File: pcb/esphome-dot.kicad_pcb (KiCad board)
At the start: 4 copper layers, 77 x 75.8 mm, 7 parts, among them J1 Input, J2 Even, J3 Odd, J4 Output, J5 SPK1, J6 SPK2

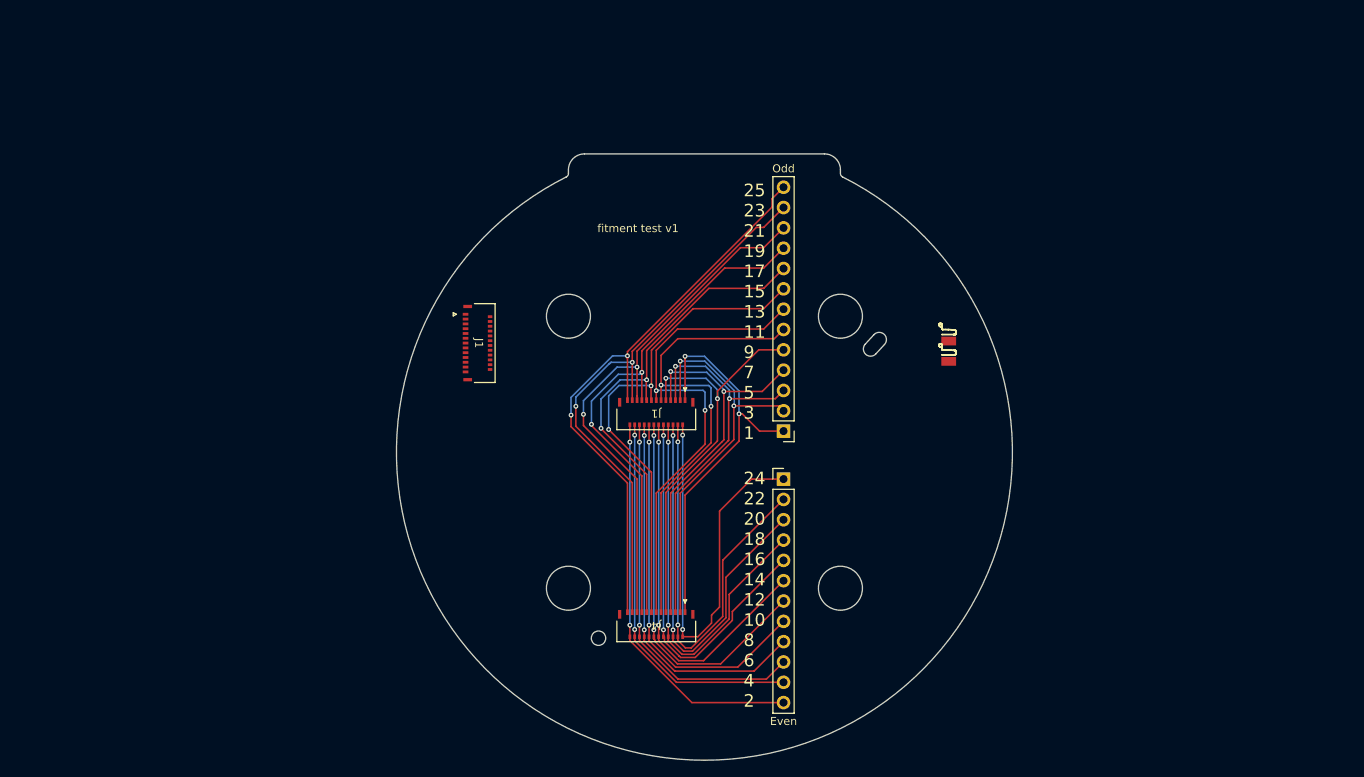
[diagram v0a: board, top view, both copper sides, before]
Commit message: pcb-fitment-v2
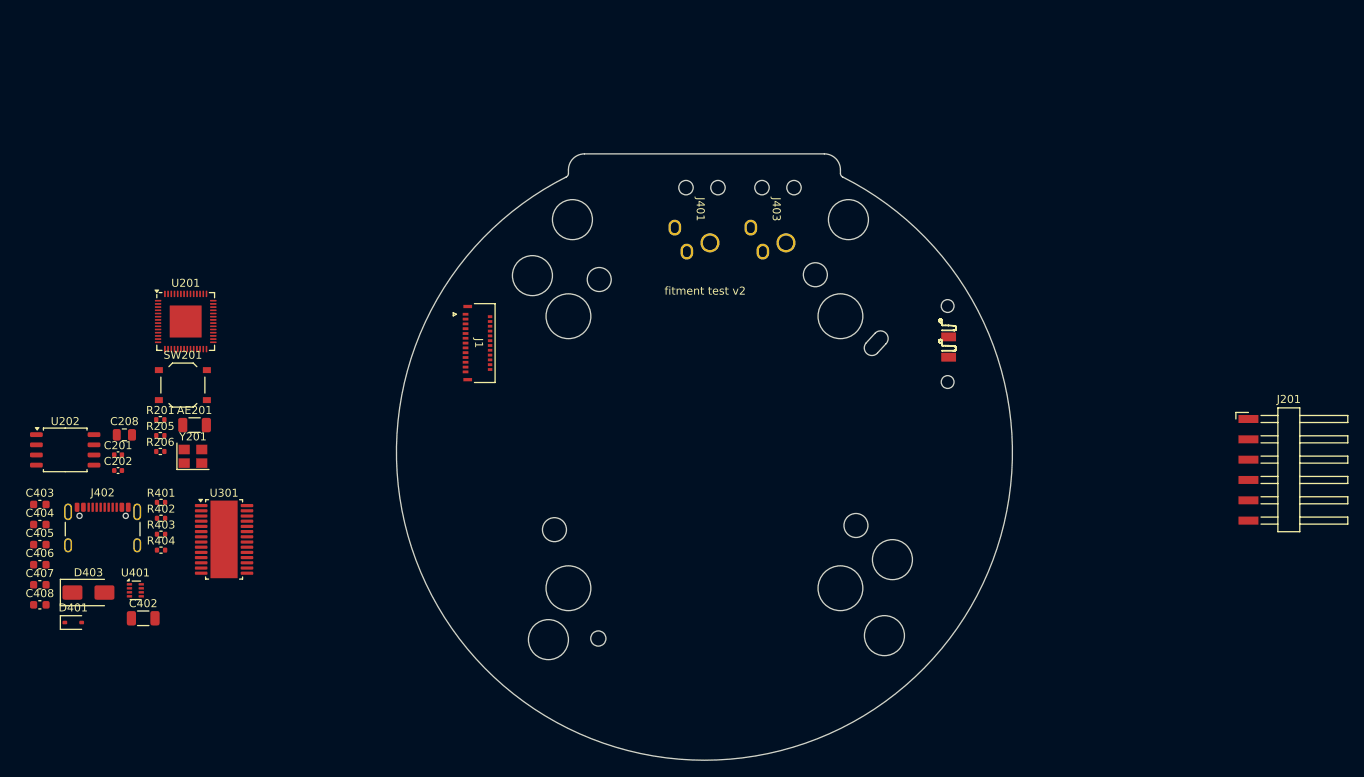
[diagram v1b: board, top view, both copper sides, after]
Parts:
- removed the J1 at (77.9, 66.6)
- removed J2: Even, Connector_PinHeader_2.54mm:PinHeader_1x12_P2.54mm_Vertical
- removed J3: Odd, Connector_PinHeader_2.54mm:PinHeader_1x13_P2.54mm_Vertical
- removed J4: Output, alexa:CONN_502598-2593_MOLEX
- added AE201: ANT3216LL00R2400A, Capacitor_SMD:C_1206_3216Metric, F.Cu at (42.4, 76.8)
- added C201: 20pF, Capacitor_SMD:C_0402_1005Metric, F.Cu at (32.8, 80.6)
- added C202: 20pF, Capacitor_SMD:C_0402_1005Metric, F.Cu at (32.8, 82.5)
- added C208: 10u, Capacitor_SMD:C_0805_2012Metric, F.Cu at (33.6, 78.1)
- added C402: 10u, Capacitor_SMD:C_1206_3216Metric, F.Cu at (36.0, 101.0)
- added C403: 100n, Capacitor_SMD:C_0603_1608Metric, F.Cu at (23.0, 86.8)
- added C404: 0.1u, Capacitor_SMD:C_0603_1608Metric, F.Cu at (23.0, 89.3)
- added C405: 10u, Capacitor_SMD:C_0603_1608Metric, F.Cu at (23.0, 91.8)
- added C406: 27p, Capacitor_SMD:C_0603_1608Metric, F.Cu at (23.0, 94.3)
- added C407: 10u, Capacitor_SMD:C_0603_1608Metric, F.Cu at (23.0, 96.8)
- added C408: 10u, Capacitor_SMD:C_0603_1608Metric, F.Cu at (23.0, 99.3)
- added D401: CUS05S40.H3F, Diode_SMD:D_SOD-323, F.Cu at (27.2, 101.5)
- added D403: SMAJ22A, Diode_SMD:D_SMA, F.Cu at (29.1, 97.8)
- added J201: eflashy32, Connector_Harwin:Harwin_M20-89006xx_1x06_P2.54mm_Horizontal, F.Cu at (179.6, 82.4)
- added J401: ADC-055B-9, !esphome-dot:BarrelJack_AdamTech_ADC-055B-9, F.Cu at (105.6, 49.2)
- added J402: USBC, Connector_USB:USB_C_Receptacle_GCT_USB4105-xx-A_16P_TopMnt_Horizontal, F.Cu at (30.9, 90.8)
- added J403: ADC-055B-9, !esphome-dot:BarrelJack_AdamTech_ADC-055B-9, F.Cu at (115.1, 49.2)
- added R201: 22, Resistor_SMD:R_0402_1005Metric, F.Cu at (38.1, 76.2)
- added R205: 10k, Resistor_SMD:R_0402_1005Metric, F.Cu at (38.1, 78.2)
- added R206: 10k, Resistor_SMD:R_0402_1005Metric, F.Cu at (38.1, 80.1)
- added R401: 5k1, Resistor_SMD:R_0402_1005Metric, F.Cu at (38.2, 86.5)
- added R402: 5k1, Resistor_SMD:R_0402_1005Metric, F.Cu at (38.2, 88.5)
- added R403: 68k, Resistor_SMD:R_0402_1005Metric, F.Cu at (38.2, 90.5)
- added R404: 22k, Resistor_SMD:R_0402_1005Metric, F.Cu at (38.2, 92.5)
- added SW201: RESET, Button_Switch_SMD:SW_Push_1P1T_XKB_TS-1187A, F.Cu at (40.9, 71.8)
- added U201: ESP32-S3R8, Package_DFN_QFN:QFN-56-1EP_7x7mm_P0.4mm_EP4x4mm, F.Cu at (41.3, 63.9)
- added U202: W25Q128JVSIQ, Package_SO:SOIC-8_5.23x5.23mm_P1.27mm, F.Cu at (26.2, 79.9)
- added U301: TAS5805M, Package_SO:TSSOP-28-1EP_4.4x9.7mm_P0.65mm_EP3.4x9.7mm_Mask3.1x4.05mm, F.Cu at (46.1, 91.1)
- added U401: TPS62932, Package_TO_SOT_SMD:SOT-583-8, F.Cu at (35.0, 97.5)
- added Y201: 40MHz, Crystal:Crystal_SMD_3225-4Pin_3.2x2.5mm, F.Cu at (42.2, 80.7)
- moved J1 23.9 mm to (77.9, 66.6), turned to -90 degrees
- moved J5 0.52 mm to (136.6, 65.8)
- moved J6 0.52 mm to (136.6, 68.4)
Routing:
- net PIN25: track 73.7 -> 0.00 mm, vias 2 -> 0
- net PIN23: track 71.1 -> 0.00 mm, vias 2 -> 0
- net PIN21: track 68.5 -> 0.00 mm, vias 2 -> 0
- net PIN19: track 66.0 -> 0.00 mm, vias 2 -> 0
- net PIN17: track 63.3 -> 0.00 mm, vias 2 -> 0
- net PIN15: track 61.1 -> 0.00 mm, vias 2 -> 0
- net PIN13: track 60.5 -> 0.00 mm, vias 2 -> 0
- net PIN11: track 59.3 -> 0.00 mm, vias 2 -> 0
- net PIN2: track 54.9 -> 0.00 mm, vias 2 -> 0
- net PIN4: track 52.4 -> 0.00 mm, vias 2 -> 0
- net PIN9: track 51.6 -> 0.00 mm, vias 2 -> 0
- net PIN6: track 51.0 -> 0.00 mm, vias 2 -> 0
- net PIN1: track 50.9 -> 0.00 mm, vias 2 -> 0
- net PIN7: track 50.3 -> 0.00 mm, vias 2 -> 0
- net PIN3: track 50.1 -> 0.00 mm, vias 2 -> 0
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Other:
- outline, holes or cut-outs redrawn
- board text added: "Antenna Here"
- board text added: "Tall Capacitor here?"
- board text added: "fitment test v2"
- board text added: "temp"
- board text removed: "24 22 20 18 16 14 12 10 8 6 4 2"
- board text removed: "25 23 21 19 17 15 13 11 9 7 5 3 1"
- board text removed: "fitment test v1"

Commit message: schematic and tweaks
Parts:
- added C203: 100n, Capacitor_SMD:C_0402_1005Metric, F.Cu at (46.0, 28.0)
- added C204: 1u, Capacitor_SMD:C_0402_1005Metric, F.Cu at (46.0, 30.0)
- added C205: 100n, Capacitor_SMD:C_0402_1005Metric, F.Cu at (46.0, 31.9)
- added C206: 10u, Capacitor_SMD:C_0603_1608Metric, F.Cu at (49.5, 28.3)
- added C207: 100n, Capacitor_SMD:C_0402_1005Metric, F.Cu at (46.0, 33.9)
- added C209: 100n, Capacitor_SMD:C_0402_1005Metric, F.Cu at (46.0, 35.9)
- added C212: 100n, Capacitor_SMD:C_0402_1005Metric, F.Cu at (46.0, 37.9)
- added C213: 100n, Capacitor_SMD:C_0402_1005Metric, F.Cu at (46.0, 39.8)
- added C214: 100n, Capacitor_SMD:C_0402_1005Metric, F.Cu at (46.0, 41.8)
- added C301: 1u, Capacitor_SMD:C_0402_1005Metric, F.Cu at (40.0, 28.0)
- added C302: 1u, Capacitor_SMD:C_0402_1005Metric, F.Cu at (40.0, 30.0)
- added C303: 100n, Capacitor_SMD:C_0402_1005Metric, F.Cu at (40.0, 31.9)
- added C304: 10u, Capacitor_SMD:C_0603_1608Metric, F.Cu at (40.6, 38.1)
- added C305: 220n, Capacitor_SMD:C_0805_2012Metric, F.Cu at (36.4, 28.5)
- added C306: 220n, Capacitor_SMD:C_0805_2012Metric, F.Cu at (36.4, 31.5)
- added C307: 220n, Capacitor_SMD:C_0805_2012Metric, F.Cu at (36.4, 34.5)
- added C308: 220n, Capacitor_SMD:C_0805_2012Metric, F.Cu at (36.4, 37.6)
- added C309: 100n, Capacitor_SMD:C_0402_1005Metric, F.Cu at (40.0, 33.9)
- added C310: 22u, Capacitor_SMD:C_0805_2012Metric, F.Cu at (36.4, 40.6)
- added C311: 680n, Capacitor_SMD:C_0805_2012Metric, F.Cu at (36.4, 43.6)
- added C312: 330u, Capacitor_SMD:CP_Elec_10x10.5, F.Cu at (27.0, 33.0)
- added C313: 680n, Capacitor_SMD:C_0805_2012Metric, F.Cu at (36.4, 46.6)
- added C314: 100n, Capacitor_SMD:C_0402_1005Metric, F.Cu at (40.0, 35.9)
- added C315: 22u, Capacitor_SMD:C_0805_2012Metric, F.Cu at (36.4, 49.6)
- added C316: 330u, Capacitor_SMD:CP_Elec_10x10.5, F.Cu at (27.0, 45.1)
- added C401: 100n, Capacitor_SMD:C_0402_1005Metric, F.Cu at (46.0, 45.8)
- added J404: 20V, Connector_PinSocket_2.54mm:PinSocket_1x02_P2.54mm_Horizontal, F.Cu at (69.0, 51.7)
- added J405: 20v, Connector_PinHeader_2.54mm:PinHeader_1x02_P2.54mm_Horizontal, F.Cu at (60.3, 44.5)
- added L201: 2nH, Inductor_SMD:L_0402_1005Metric, F.Cu at (48.9, 30.5)
- C208: footprint Capacitor_SMD:C_0805_2012Metric -> Capacitor_SMD:C_0603_1608Metric
- C402: footprint Capacitor_SMD:C_1206_3216Metric -> Capacitor_SMD:C_0805_2012Metric
- C403: footprint Capacitor_SMD:C_0603_1608Metric -> Capacitor_SMD:C_0402_1005Metric
- C404: value 0.1u -> 100n; footprint Capacitor_SMD:C_0603_1608Metric -> Capacitor_SMD:C_0402_1005Metric
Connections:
- J401 pad 1: +20V -> Net-(J404-Pin_1)
- U301 pad 15: PVDD -> +20V
- U301 pad 16: PVDD -> +20V
- U301 pad 27: PVDD -> +20V
- U301 pad 28: PVDD -> +20V
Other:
- outline, holes or cut-outs redrawn
- board text added: "<<hash>>"
- board text added: "Inductors 3.85mm max height"
- board text added: "fitment test v3"
- board text added: "shipping shield"
- board text removed: "fitment test v2"
